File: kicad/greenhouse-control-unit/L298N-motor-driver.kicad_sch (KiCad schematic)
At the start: 14 parts, among them U3 L298HN

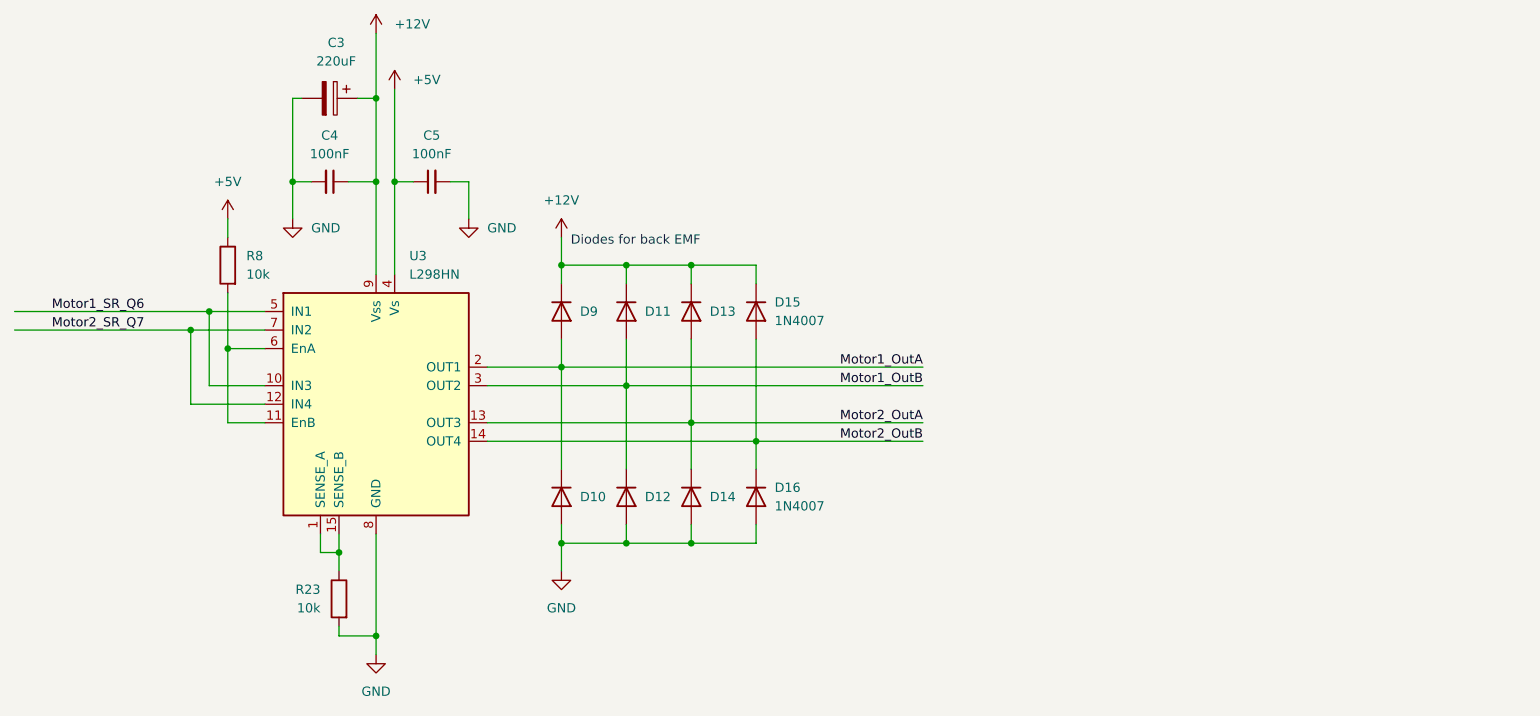
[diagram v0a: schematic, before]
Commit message: Add voltage regulator to motor driver
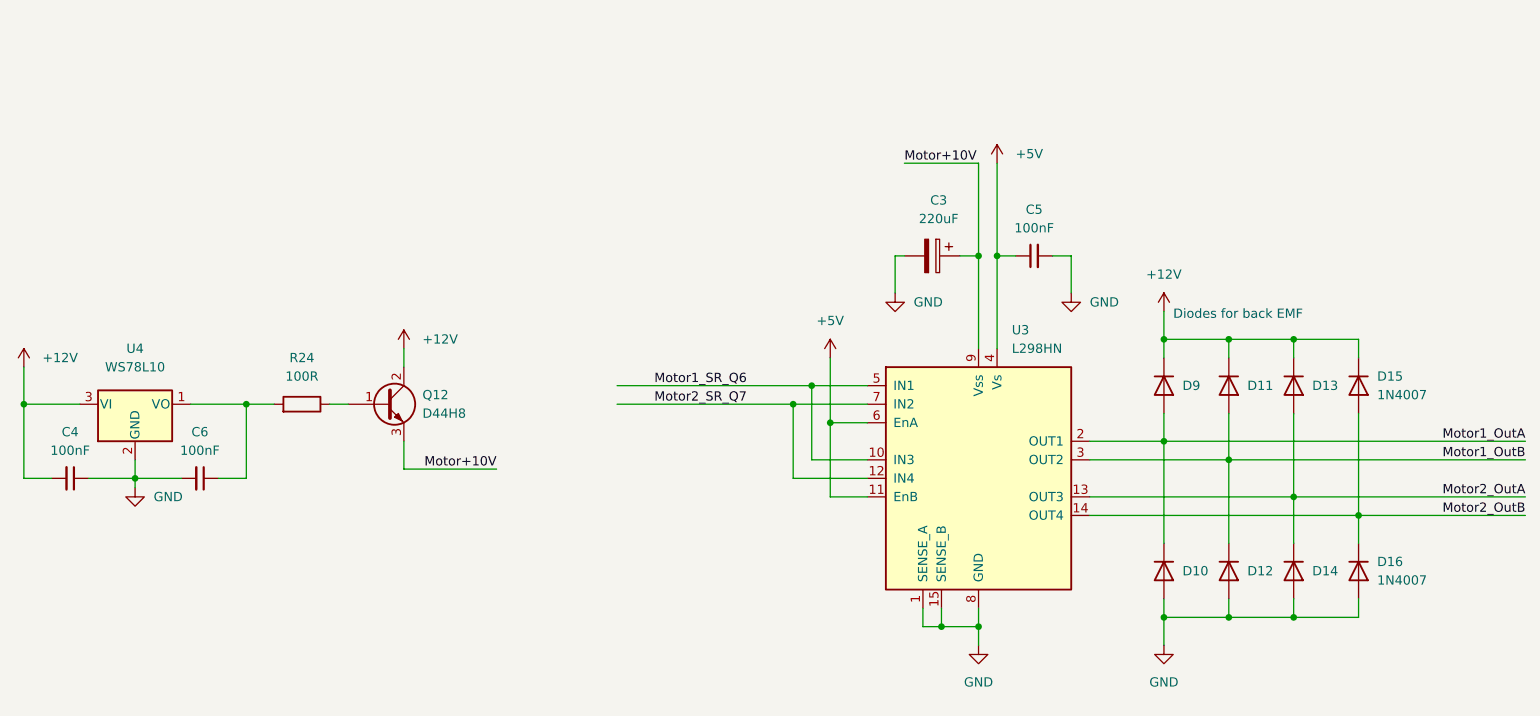
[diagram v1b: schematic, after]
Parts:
- removed R23, R8: 10k, Resistor_THT:R_Axial_DIN0204_L3.6mm_D1.6mm_P5.08mm_Horizontal, symbol Device:R
- added C6: 100nF, Capacitor_THT:C_Disc_D4.7mm_W2.5mm_P5.00mm, symbol Device:C_Small
- added Q12: D44H8, Package_TO_SOT_THT:TO-220-3_Vertical, symbol Transistor_BJT:BD911
- added R24: 100R, Resistor_THT:R_Axial_DIN0204_L3.6mm_D1.6mm_P5.08mm_Horizontal, symbol Device:R
- added U4: WS78L10, Nick:TO-92L_Inline_China, symbol Regulator_Linear:L78L10_TO92
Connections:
- net +12V: now also C4.2, Q12.2 (C), U4.3 (VI); no longer C3.1, C4.1, U3.9 (Vss)
- net +5V: now also U3.11 (EnB), U3.6 (EnA)
- net GND: now also C4.1, U3.1 (SENSE_A), U3.15 (SENSE_B), C6.2, U4.2 (GND); no longer C4.2
- new net: C6.1, R24.2, U4.1 (VO)
- new net: Q12.1 (B), R24.1
- new net Motor+10V: C3.1, Q12.3 (E), U3.9 (Vss)
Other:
- moved on the sheet: C3, C5, D10, D11, D12, D13, D14, D15, D16, D9, U3

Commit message: Change cap for motor driver regulator
Also moved battery coil to PSU #236
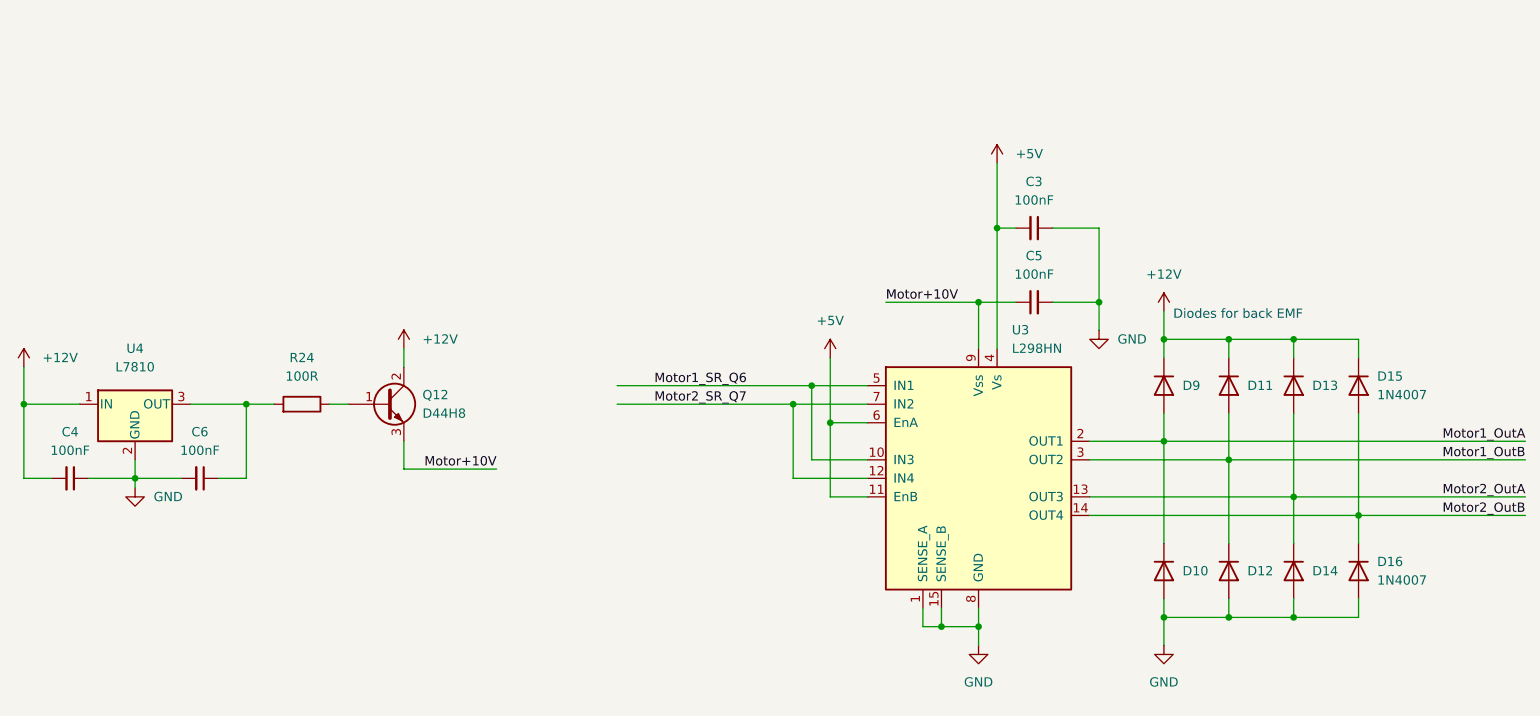
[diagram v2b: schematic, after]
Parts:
- removed C3: 220uF, Capacitor_THT:CP_Radial_D6.3mm_P2.50mm, symbol Device:C_Polarized
- removed U4: WS78L10, Nick:TO-92L_Inline_China, symbol Regulator_Linear:L78L10_TO92
- added C3: 100nF, Capacitor_THT:C_Disc_D4.7mm_W2.5mm_P5.00mm, symbol Device:C_Small
- added U4: L7810, symbol Regulator_Linear:L7809
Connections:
- net +12V: now also U4.1 (IN)
- net +5V: now also C3.2; no longer C5.1
- net GND: now also C3.1, U4.2 (GND)
- net Motor+10V: now also C5.1
- net at C6.1, R24.2: now also U4.3 (OUT)
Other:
- moved on the sheet: C5

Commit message: Add reverse voltage diode and re-draw ground plane
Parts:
- U3: renamed from U4; footprint (none) -> Nick:TO-92L_Inline_Regulator
- renumbered C4 to C3, C6 to C4, C3 to C5, C5 to C6, D9 to D10, D10 to D11, D11 to D12, D12 to D13, D13 to D14, D14 to D15, D15 to D16, D16 to D17, R24 to R22, U3 to U4
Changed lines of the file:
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@@
   (symbol (lib_id "Device:C_Small") (at 175.26 60.96 270) (unit 1)
     (in_bom yes) (on_board yes) (fields_autoplaced)
-    (property "Reference" "C3" (id 0) (at 175.2536 54.61 90))
+    (property "Reference" "C5" (id 0) (at 175.2536 54.61 90))
     (property "Value" "100nF" (id 1) (at 175.2536 57.15 90))
     (property "Footprint" "Capacitor_THT:C_Disc_D4.7mm_W2.5mm_P5.00mm" (id 2) (at 175.26 60.96 0)
@@
   (symbol (lib_id "power:GND") (at 184.15 74.93 0) (unit 1)
     (in_bom yes) (on_board yes) (fields_autoplaced)
-    (property "Reference" "#PWR0108" (id 0) (at 184.15 81.28 0)
+    (property "Reference" "#PWR050" (id 0) (at 184.15 81.28 0)
       (effects (font (size 1.27 1.27)) hide)
     )
@@
   (symbol (lib_id "Device:C_Small") (at 43.18 95.25 270) (unit 1)
     (in_bom yes) (on_board yes) (fields_autoplaced)
-    (property "Reference" "C4" (id 0) (at 43.1736 88.9 90))
+    (property "Reference" "C3" (id 0) (at 43.1736 88.9 90))
     (property "Value" "100nF" (id 1) (at 43.1736 91.44 90))
     (property "Footprint" "Capacitor_THT:C_Disc_D4.7mm_W2.5mm_P5.00mm" (id 2) (at 43.18 95.25 0)
@@
   (symbol (lib_id "Diode:1N4007") (at 201.93 107.95 270) (unit 1)
     (in_bom yes) (on_board yes) (fields_autoplaced)
-    (property "Reference" "D12" (id 0) (at 204.47 107.9499 90)
+    (property "Reference" "D13" (id 0) (at 204.47 107.9499 90)
       (effects (font (size 1.27 1.27)) (justify left))
     )
@@
   (symbol (lib_id "Diode:1N4007") (at 210.82 107.95 270) (unit 1)
     (in_bom yes) (on_board yes) (fields_autoplaced)
-    (property "Reference" "D14" (id 0) (at 213.36 107.9499 90)
+    (property "Reference" "D15" (id 0) (at 213.36 107.9499 90)
       (effects (font (size 1.27 1.27)) (justify left))
     )
@@
   (symbol (lib_id "Regulator_Linear:L7809") (at 52.07 85.09 0) (unit 1)
     (in_bom yes) (on_board yes) (fields_autoplaced)
-    (property "Reference" "U4" (id 0) (at 52.07 77.47 0))
+    (property "Reference" "U3" (id 0) (at 52.07 77.47 0))
     (property "Value" "L7810" (id 1) (at 52.07 80.01 0))
-    (property "Footprint" "" (id 2) (at 52.705 88.9 0)
+    (property "Footprint" "Nick:TO-92L_Inline_Regulator" (id 2) (at 52.705 88.9 0)
       (effects (font (size 1.27 1.27) italic) (justify left) hide)
     )
@@
   (symbol (lib_id "Diode:1N4007") (at 219.71 82.55 270) (unit 1)
     (in_bom yes) (on_board yes) (fields_autoplaced)
-    (property "Reference" "D15" (id 0) (at 222.25 81.2799 90)
+    (property "Reference" "D16" (id 0) (at 222.25 81.2799 90)
       (effects (font (size 1.27 1.27)) (justify left))
     )
@@
   (symbol (lib_id "Device:C_Small") (at 60.96 95.25 270) (unit 1)
     (in_bom yes) (on_board yes) (fields_autoplaced)
-    (property "Reference" "C6" (id 0) (at 60.9536 88.9 90))
+    (property "Reference" "C4" (id 0) (at 60.9536 88.9 90))
     (property "Value" "100nF" (id 1) (at 60.9536 91.44 90))
     (property "Footprint" "Capacitor_THT:C_Disc_D4.7mm_W2.5mm_P5.00mm" (id 2) (at 60.96 95.25 0)
@@
   (symbol (lib_id "power:GND") (at 167.64 118.11 0) (unit 1)
     (in_bom yes) (on_board yes) (fields_autoplaced)
-    (property "Reference" "#PWR0102" (id 0) (at 167.64 124.46 0)
+    (property "Reference" "#PWR048" (id 0) (at 167.64 124.46 0)
       (effects (font (size 1.27 1.27)) hide)
     )
@@
   (symbol (lib_id "Diode:1N4007") (at 193.04 107.95 270) (unit 1)
     (in_bom yes) (on_board yes) (fields_autoplaced)
-    (property "Reference" "D10" (id 0) (at 195.58 107.9499 90)
+    (property "Reference" "D11" (id 0) (at 195.58 107.9499 90)
       (effects (font (size 1.27 1.27)) (justify left))
     )
@@
   (symbol (lib_id "Device:R") (at 74.93 85.09 270) (mirror x) (unit 1)
     (in_bom yes) (on_board yes) (fields_autoplaced)
-    (property "Reference" "R24" (id 0) (at 74.93 78.74 90))
+    (property "Reference" "R22" (id 0) (at 74.93 78.74 90))
     (property "Value" "100R" (id 1) (at 74.93 81.28 90))
     (property "Footprint" "Resistor_THT:R_Axial_DIN0204_L3.6mm_D1.6mm_P5.08mm_Horizontal" (id 2) (at 74.93 86.868 90)
@@
   (symbol (lib_id "power:+12V") (at 88.9 77.47 0) (unit 1)
     (in_bom yes) (on_board yes) (fields_autoplaced)
-    (property "Reference" "#PWR028" (id 0) (at 88.9 81.28 0)
+    (property "Reference" "#PWR046" (id 0) (at 88.9 81.28 0)
       (effects (font (size 1.27 1.27)) hide)
     )
@@
   (symbol (lib_id "Diode:1N4007") (at 219.71 107.95 270) (unit 1)
     (in_bom yes) (on_board yes) (fields_autoplaced)
-    (property "Reference" "D16" (id 0) (at 222.25 106.6799 90)
+    (property "Reference" "D17" (id 0) (at 222.25 106.6799 90)
       (effects (font (size 1.27 1.27)) (justify left))
     )
@@
   (symbol (lib_id "power:+12V") (at 36.83 80.01 0) (unit 1)
     (in_bom yes) (on_board yes) (fields_autoplaced)
-    (property "Reference" "#PWR07" (id 0) (at 36.83 83.82 0)
+    (property "Reference" "#PWR044" (id 0) (at 36.83 83.82 0)
       (effects (font (size 1.27 1.27)) hide)
     )
@@
   (symbol (lib_id "Diode:1N4007") (at 193.04 82.55 270) (unit 1)
     (in_bom yes) (on_board yes) (fields_autoplaced)
-    (property "Reference" "D9" (id 0) (at 195.58 82.5499 90)
+    (property "Reference" "D10" (id 0) (at 195.58 82.5499 90)
       (effects (font (size 1.27 1.27)) (justify left))
     )
@@
   (symbol (lib_id "power:+5V") (at 170.18 52.07 0) (unit 1)
     (in_bom yes) (on_board yes) (fields_autoplaced)
-    (property "Reference" "#PWR0107" (id 0) (at 170.18 55.88 0)
+    (property "Reference" "#PWR049" (id 0) (at 170.18 55.88 0)
       (effects (font (size 1.27 1.27)) hide)
     )
@@
   (symbol (lib_id "Driver_Motor:L298HN") (at 167.64 95.25 0) (unit 1)
     (in_bom yes) (on_board yes) (fields_autoplaced)
-    (property "Reference" "U3" (id 0) (at 172.1994 74.93 0)
+    (property "Reference" "U4" (id 0) (at 172.1994 74.93 0)
       (effects (font (size 1.27 1.27)) (justify left))
     )
@@
   (symbol (lib_id "power:GND") (at 193.04 118.11 0) (unit 1)
     (in_bom yes) (on_board yes) (fields_autoplaced)
-    (property "Reference" "#PWR0103" (id 0) (at 193.04 124.46 0)
+    (property "Reference" "#PWR052" (id 0) (at 193.04 124.46 0)
       (effects (font (size 1.27 1.27)) hide)
     )
@@
   (symbol (lib_id "Diode:1N4007") (at 210.82 82.55 270) (unit 1)
     (in_bom yes) (on_board yes) (fields_autoplaced)
-    (property "Reference" "D13" (id 0) (at 213.36 82.5499 90)
+    (property "Reference" "D14" (id 0) (at 213.36 82.5499 90)
       (effects (font (size 1.27 1.27)) (justify left))
     )
@@
   (symbol (lib_id "Device:C_Small") (at 175.26 71.12 90) (unit 1)
     (in_bom yes) (on_board yes) (fields_autoplaced)
-    (property "Reference" "C5" (id 0) (at 175.2663 64.77 90))
+    (property "Reference" "C6" (id 0) (at 175.2663 64.77 90))
     (property "Value" "100nF" (id 1) (at 175.2663 67.31 90))
     (property "Footprint" "Capacitor_THT:C_Disc_D4.7mm_W2.5mm_P5.00mm" (id 2) (at 175.26 71.12 0)
@@
   (symbol (lib_id "Diode:1N4007") (at 201.93 82.55 270) (unit 1)
     (in_bom yes) (on_board yes) (fields_autoplaced)
-    (property "Reference" "D11" (id 0) (at 204.47 82.5499 90)
+    (property "Reference" "D12" (id 0) (at 204.47 82.5499 90)
       (effects (font (size 1.27 1.27)) (justify left))
     )
@@
   (symbol (lib_id "power:GND") (at 52.07 96.52 0) (unit 1)
     (in_bom yes) (on_board yes) (fields_autoplaced)
-    (property "Reference" "#PWR024" (id 0) (at 52.07 102.87 0)
+    (property "Reference" "#PWR045" (id 0) (at 52.07 102.87 0)
       (effects (font (size 1.27 1.27)) hide)
     )
@@
   (symbol (lib_id "power:+12V") (at 193.04 72.39 0) (unit 1)
     (in_bom yes) (on_board yes) (fields_autoplaced)
-    (property "Reference" "#PWR0109" (id 0) (at 193.04 76.2 0)
+    (property "Reference" "#PWR051" (id 0) (at 193.04 76.2 0)
       (effects (font (size 1.27 1.27)) hide)
     )
@@
   (symbol (lib_id "power:+5V") (at 147.32 78.74 0) (unit 1)
     (in_bom yes) (on_board yes) (fields_autoplaced)
-    (property "Reference" "#PWR0104" (id 0) (at 147.32 82.55 0)
-      (effects (font (size 1.27 1.27)) hide)
-    )
+    (property "Reference" "#PWR047" (id 0) (at 147.32 82.55 0)
+      (effects (font (size 1.27 1.27)) hide)
+    )
